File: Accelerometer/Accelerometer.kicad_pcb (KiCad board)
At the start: 2 copper layers, 39.9 x 9.6 mm, 13 parts, among them J1 Conn_01x08_Pin, U1 DA14531_17-ball_WLCSP, Y1 Crystal_GND24

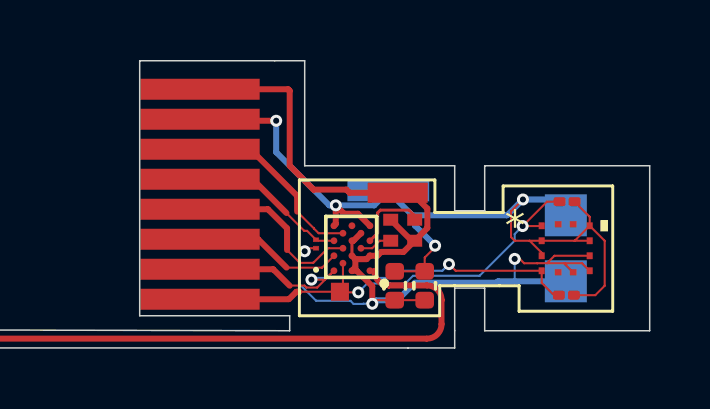
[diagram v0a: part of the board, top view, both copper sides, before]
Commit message: updated PCB with correct pin connections
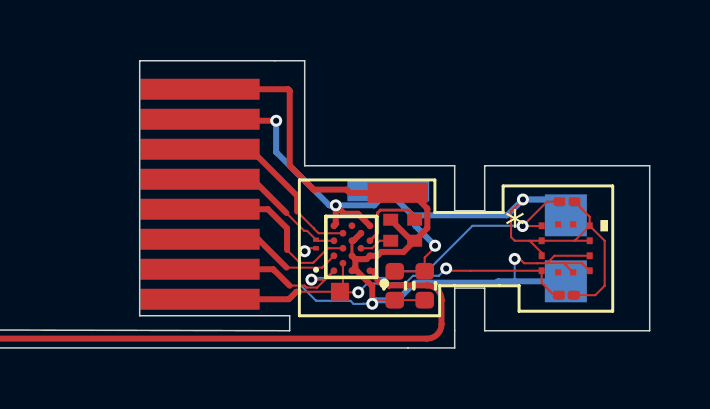
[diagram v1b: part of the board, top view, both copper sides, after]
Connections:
- REF** pad 1: Net-(J1-Pin_1) -> Net-(J1-Pin_2) (x2)
- REF** pad 4: Net-(J1-Pin_2) -> Net-(J1-Pin_1)
- REF** pad 1: Net-(J1-Pin_2) -> Net-(J1-Pin_1)
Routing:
- net Net-(J1-Pin_1): track 15.4 -> 14.2 mm
- net Net-(J1-Pin_2): track 15.0 -> 15.8 mm

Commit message: Double checked schematic
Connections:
- REF** pad 3: /+VE -> /GND
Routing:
- net Net-(U1-RFIOp): track 34.2 -> 35.3 mm
- net /+VE: track 30.7 -> 30.1 mm
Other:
- board size 39.9 x 9.6 mm -> 45 x 9 mm
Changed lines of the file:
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@@
 			(size 0.2286 0.2032)
 			(layers "F.Cu" "F.Mask" "F.Paste")
-			(net 1 "/+VE")
+			(net 2 "/GND")
 		)
 		(pad "4" smd rect
@@
 	)
 	(gr_arc
-		(start 139.579016 115.989634)
-		(mid 139.921718 116.132433)
-		(end 140.061623 116.476326)
+		(start 141.466581 115.988321)
+		(mid 141.906176 116.171496)
+		(end 142.085662 116.61261)
 		(stroke
 			(width 0.2)
@@
 	)
 	(gr_arc
-		(start 140.060827 117.279506)
-		(mid 139.918028 117.622208)
-		(end 139.574135 117.762113)
+		(start 142.566543 117.125834)
+		(mid 142.223844 116.983033)
+		(end 142.083936 116.639142)
 		(stroke
 			(width 0.2)
@@
 	)
 	(gr_line
-		(start 141.5 117.5)
-		(end 141.5 116.079636)
+		(start 146.013204 116.845168)
+		(end 146.013204 112)
 		(stroke
 			(width 0.05)
@@
 	)
 	(gr_line
-		(start 138.94685 118.073093)
-		(end 140.5 118.073093)
-		(stroke
-			(width 0.05)
-			(type default)
-		)
-		(layer "Edge.Cuts")
-	)
-	(gr_line
-		(start 107.05685 118.073093)
-		(end 107.05685 117.433093)
+		(start 141.5 116.5)
+		(end 140.5 116.5)
 		(stroke
 			(width 0.05)
@@
 	)
 	(gr_line
-		(start 140.5 113.5)
-		(end 141.5 113.5)
+		(start 141.5 112)
+		(end 146.013204 112)
 		(stroke
 			(width 0.05)
@@
 	)
 	(gr_line
-		(start 140.5 112)
-		(end 140.5 113.5)
+		(start 135 117.5)
+		(end 130 117.5)
 		(stroke
 			(width 0.05)
@@
 	)
 	(gr_line
-		(start 140.5 116.079636)
-		(end 140.5 117.5)
+		(start 140.5 113.5)
+		(end 141.5 113.5)
 		(stroke
 			(width 0.05)
@@
 	(gr_line
 		(start 147 117.5)
-		(end 141.5 117.5)
+		(end 175 117.5)
 		(stroke
 			(width 0.05)
@@
 	)
 	(gr_line
-		(start 134.5 108.5)
-		(end 135.5 108.5)
+		(start 175 116.836335)
+		(end 146.013204 116.845168)
 		(stroke
 			(width 0.05)
@@
 	)
 	(gr_line
-		(start 130 108.5)
-		(end 134.5 108.5)
+		(start 140.5 112)
+		(end 140.5 113.5)
 		(stroke
 			(width 0.05)
@@
 	)
 	(gr_line
-		(start 130 117)
-		(end 135 117)
+		(start 147 117.5)
+		(end 141.5 117.5)
 		(stroke
 			(width 0.05)
@@
 	)
 	(gr_line
-		(start 141.5 116.079636)
-		(end 140.5 116.079636)
+		(start 134.5 108.5)
+		(end 135.5 108.5)
 		(stroke
 			(width 0.05)
@@
 	)
 	(gr_line
-		(start 141.5 112)
-		(end 147 112)
+		(start 175 117.5)
+		(end 175 116.836335)
 		(stroke
 			(width 0.05)
@@
 	)
 	(gr_line
-		(start 135.5 108.5)
-		(end 135.5 112)
+		(start 130 108.5)
+		(end 134.5 108.5)
 		(stroke
 			(width 0.05)
@@
 	)
 	(gr_line
-		(start 135 117)
-		(end 135 117.5)
+		(start 140.5 116.5)
+		(end 140.5 117.5)
 		(stroke
 			(width 0.05)
@@
 	)
 	(gr_line
-		(start 140.5 118.073093)
-		(end 140.5 117.5)
+		(start 135.5 108.5)
+		(end 135.5 112)
 		(stroke
 			(width 0.05)
@@
 	)
 	(gr_line
-		(start 141.5 113.5)
-		(end 141.5 112)
+		(start 140.5 117.5)
+		(end 135 117.5)
 		(stroke
 			(width 0.05)
@@
 	)
 	(gr_line
-		(start 135 117.5)
-		(end 107.05685 117.433093)
+		(start 130 117.5)
+		(end 130 117)
 		(stroke
 			(width 0.05)
@@
 	)
 	(gr_line
-		(start 147 112)
-		(end 147 117.5)
+		(start 141.5 113.5)
+		(end 141.5 112)
 		(stroke
 			(width 0.05)
@@
 	)
 	(gr_line
-		(start 138.94685 118.073093)
-		(end 107.05685 118.073093)
+		(start 141.5 117.5)
+		(end 141.5 116.5)
 		(stroke
 			(width 0.05)
@@
 	)
 	(segment
-		(start 143.3998 114.8998)
-		(end 143 114.5)
-		(width 0.07)
-		(layer "F.Cu")
-		(net 1)
-	)
-	(segment
 		(start 136.534973 113.940027)
 		(end 136.475 114)
@@
 	)
 	(segment
-		(start 143.3998 115)
-		(end 143.3998 114.8998)
-		(width 0.07)
-		(layer "F.Cu")
-		(net 1)
-	)
-	(segment
 		(start 144.473063 116.314755)
 		(end 145.185245 116.314755)
@@
 	)
 	(segment
+		(start 143.3998 115.1002)
+		(end 143.251592 115.248408)
+		(width 0.07)
+		(layer "F.Cu")
+		(net 2)
+	)
+	(segment
 		(start 139.16742 114.499222)
 		(end 139.58842 114.078222)
@@
 	)
 	(segment
+		(start 143.3998 115)
+		(end 143.3998 115.1002)
+		(width 0.07)
+		(layer "F.Cu")
+		(net 2)
+	)
+	(segment
 		(start 137.1885 115.1135)
 		(end 137.5615 115.1135)
@@
 	)
 	(segment
-		(start 138.307436 115.989634)
-		(end 138.305223 115.987421)
+		(start 142.550277 117.129864)
+		(end 174.663602 117.129864)
 		(width 0.2)
 		(layer "F.Cu")
@@
 	)
 	(segment
-		(start 140.060827 117.279506)
-		(end 140.060827 116.477122)
+		(start 138.307436 115.989634)
+		(end 141.489634 115.989634)
 		(width 0.2)
 		(layer "F.Cu")
@@
 	)
 	(segment
-		(start 139.579016 115.989634)
+		(start 138.305223 115.987421)
 		(end 138.307436 115.989634)
 		(width 0.2)
 		(layer "F.Cu")
-		(net 11)
-	)
-	(segment
-		(start 139.554152 117.762208)
-		(end 107.440827 117.762208)
-		(width 0.2)
-		(layer "F.Cu")
-		(net 11)
-	)
-	(segment
-		(start 140.060827 116.477122)
-		(end 140.061623 116.476326)
-		(width 0.2)
-		(layer "F.Cu")
